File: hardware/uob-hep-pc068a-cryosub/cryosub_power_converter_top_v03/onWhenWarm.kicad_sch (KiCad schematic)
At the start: 15 parts, among them Q2 IRLML2402TRPBF

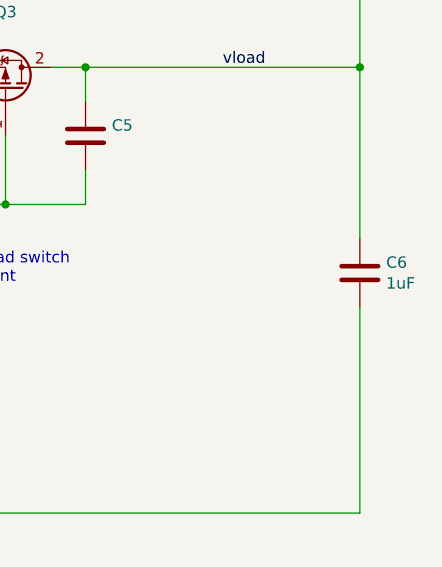
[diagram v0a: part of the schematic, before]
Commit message: Tweaked layout to remove DRCs (mainly silk) removed duplicate D1
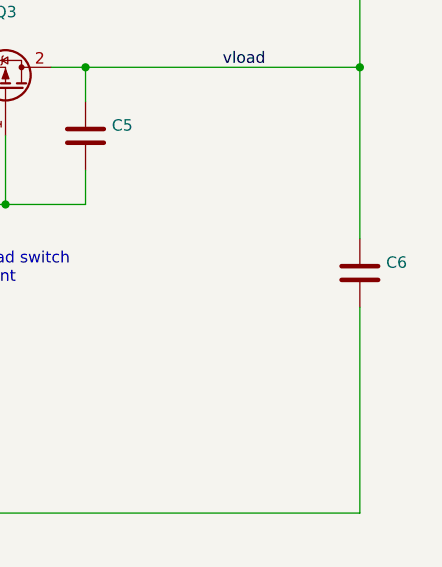
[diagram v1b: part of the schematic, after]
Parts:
- C5: footprint Capacitor_SMD:C_0603_1608Metric_Pad1.08x0.95mm_HandSolder -> (none)
- C6: value 1uF -> (none); footprint Capacitor_SMD:C_0805_2012Metric_Pad1.18x1.45mm_HandSolder -> (none)
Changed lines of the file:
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@@
       (effects (font (size 1.27 1.27)) (justify left))
     )
-    (property "Value" "1uF" (id 1) (at 267.081 97.663 0)
+    (property "Value" "" (id 1) (at 267.081 97.663 0)
       (effects (font (size 1.27 1.27)) (justify left))
     )
-    (property "Footprint" "Capacitor_SMD:C_0805_2012Metric_Pad1.18x1.45mm_HandSolder" (id 2) (at 265.1252 100.33 0)
+    (property "Footprint" "" (id 2) (at 265.1252 100.33 0)
       (effects (font (size 1.27 1.27)) hide)
     )
@@
       (effects (font (size 1.27 1.27)) (justify left))
     )
-    (property "Footprint" "Capacitor_SMD:C_0603_1608Metric_Pad1.08x0.95mm_HandSolder" (id 2) (at 234.6452 85.09 0)
+    (property "Footprint" "" (id 2) (at 234.6452 85.09 0)
       (effects (font (size 1.27 1.27)) hide)
     )

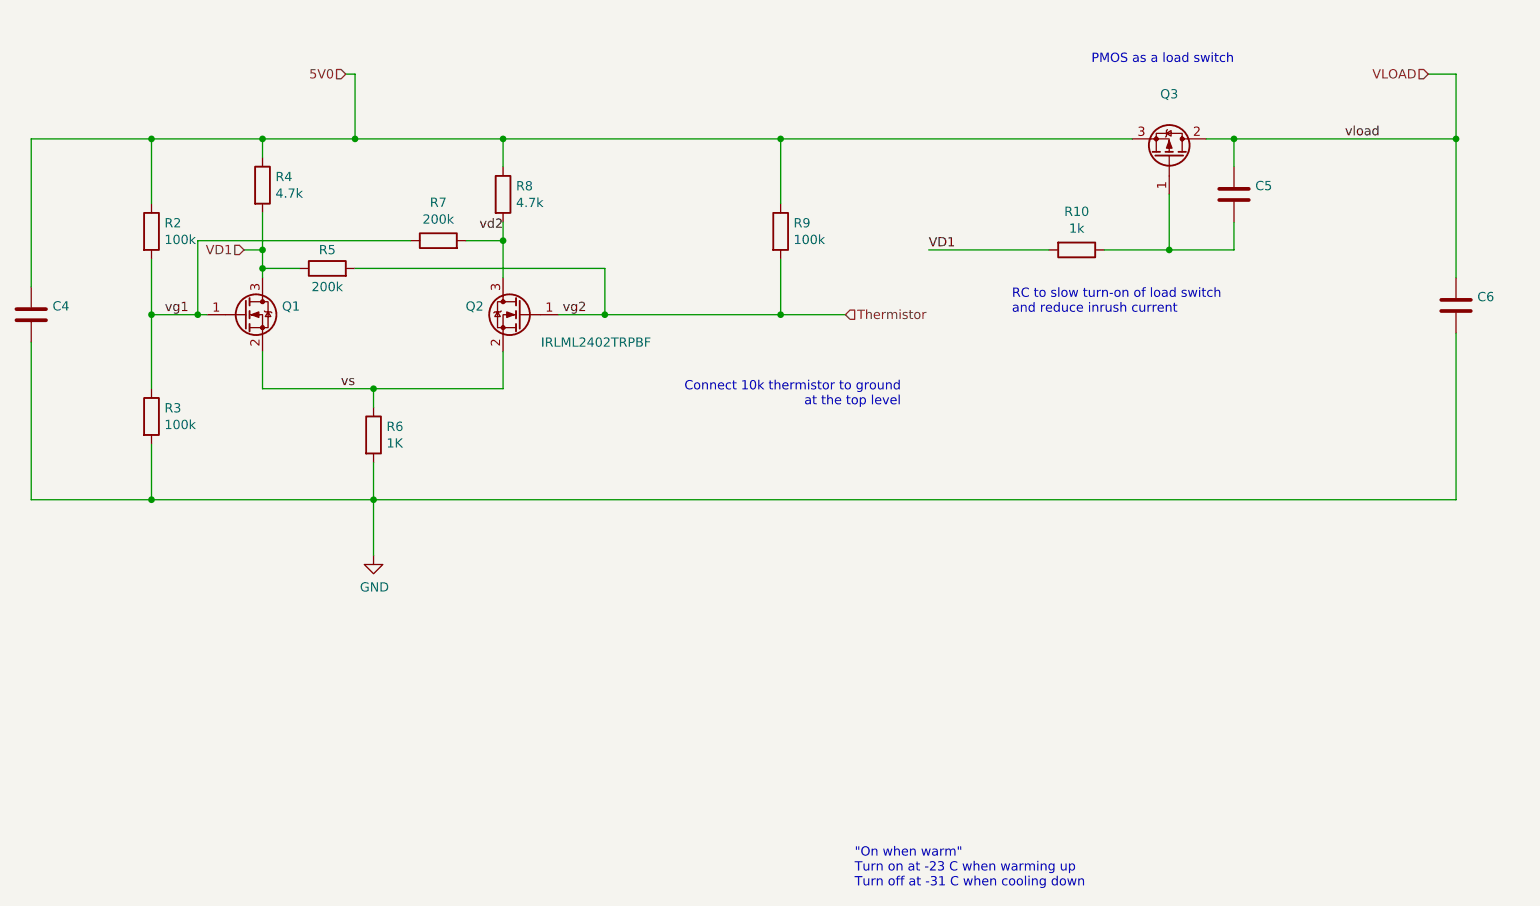
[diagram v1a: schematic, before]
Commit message: Replacing FDD306 with SiS407
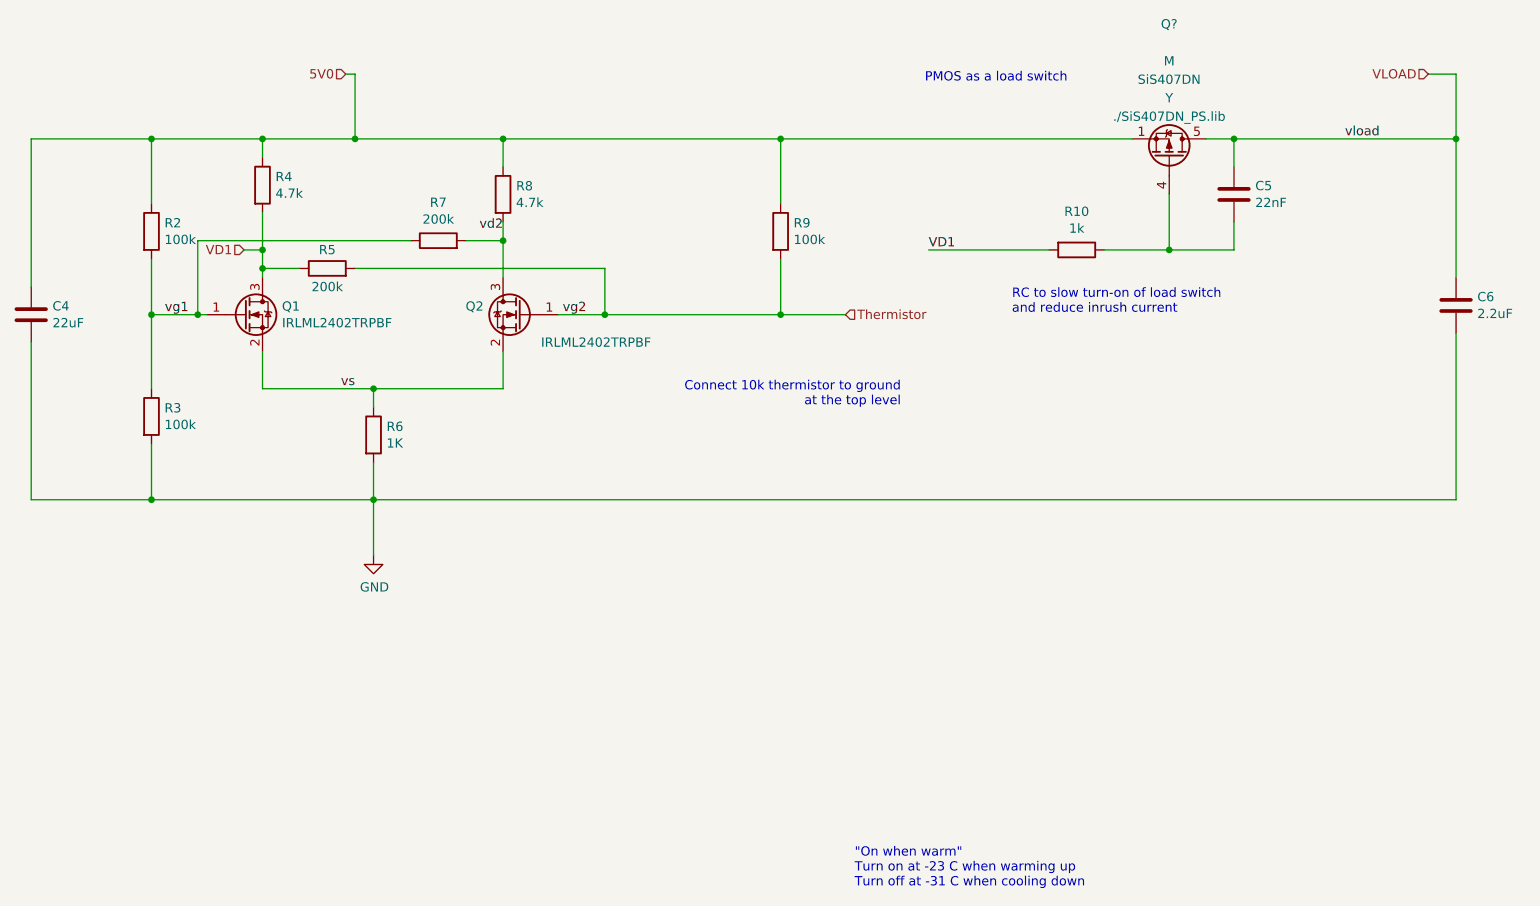
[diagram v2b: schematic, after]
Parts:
- removed Q3: (no value), symbol Device:Q_PMOS_GDS
- added Q?: (no value), symbol MOSFET:SiS407DN
- C4: value (none) -> 22uF; footprint (none) -> Capacitor_SMD:C_0805_2012Metric_Pad1.18x1.45mm_HandSolder
- C5: value (none) -> 22nF; footprint (none) -> Capacitor_SMD:C_0603_1608Metric
- C6: value (none) -> 2.2uF; footprint (none) -> Capacitor_SMD:C_0603_1608Metric
- Q1: value (none) -> IRLML2402TRPBF; footprint (none) -> Package_TO_SOT_SMD:SOT-23
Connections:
- net 5V0: now also Q?.1 (S), Q?.2 (S), Q?.3 (S)
- net VLOAD: now also Q?.5 (D)
- net at C5.2, R10.1: now also Q?.4 (G)
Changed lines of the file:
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@@
     (effects (font (size 1.27 1.27)) (justify right bottom))
   )
-  (text "PMOS as a load switch" (at 233.68 63.5 180)
+  (text "PMOS as a load switch" (at 210.82 66.04 180)
     (effects (font (size 1.27 1.27)) (justify right bottom))
   )
@@
       (effects (font (size 1.27 1.27)) (justify left))
     )
-    (property "Value" "" (id 1) (at 267.081 97.663 0)
-      (effects (font (size 1.27 1.27)) (justify left))
-    )
-    (property "Footprint" "" (id 2) (at 265.1252 100.33 0)
+    (property "Value" "2.2uF" (id 1) (at 267.081 97.663 0)
+      (effects (font (size 1.27 1.27)) (justify left))
+    )
+    (property "Footprint" "Capacitor_SMD:C_0603_1608Metric" (id 2) (at 265.1252 100.33 0)
       (effects (font (size 1.27 1.27)) hide)
     )
@@
       (effects (font (size 1.27 1.27)) (justify left))
     )
-    (property "Value" "" (id 1) (at 236.601 82.423 0)
-      (effects (font (size 1.27 1.27)) (justify left))
-    )
-    (property "Footprint" "" (id 2) (at 234.6452 85.09 0)
+    (property "Value" "22nF" (id 1) (at 236.601 82.423 0)
+      (effects (font (size 1.27 1.27)) (justify left))
+    )
+    (property "Footprint" "Capacitor_SMD:C_0603_1608Metric" (id 2) (at 234.6452 85.09 0)
       (effects (font (size 1.27 1.27)) hide)
     )
@@
       (effects (font (size 1.27 1.27)) (justify left))
     )
-    (property "Value" "" (id 1) (at 71.501 98.933 0)
-      (effects (font (size 1.27 1.27)) (justify left))
-    )
-    (property "Footprint" "" (id 2) (at 69.5452 101.6 0)
+    (property "Value" "22uF" (id 1) (at 71.501 98.933 0)
+      (effects (font (size 1.27 1.27)) (justify left))
+    )
+    (property "Footprint" "Capacitor_SMD:C_0805_2012Metric_Pad1.18x1.45mm_HandSolder" (id 2) (at 69.5452 101.6 0)
       (effects (font (size 1.27 1.27)) hide)
     )
@@
       (effects (font (size 1.27 1.27)) (justify left))
     )
-    (property "Value" "" (id 1) (at 102.997 98.933 0)
-      (effects (font (size 1.27 1.27)) (justify left))
-    )
-    (property "Footprint" "" (id 2) (at 102.87 99.695 0)
+    (property "Value" "IRLML2402TRPBF" (id 1) (at 102.997 98.933 0)
+      (effects (font (size 1.27 1.27)) (justify left))
+    )
+    (property "Footprint" "Package_TO_SOT_SMD:SOT-23" (id 2) (at 102.87 99.695 0)
       (effects (font (size 1.27 1.27) italic) (justify left) hide)
     )
@@
     (pin "2")
   )
-  (symbol (lib_id "Device:Q_PMOS_GDS") (at 224.79 76.2 270) (mirror x) (unit 1)
-    (in_bom yes) (on_board yes)
-    (property "Reference" "Q3" (id 0) (at 224.79 67.5132 90))
-    (property "Value" "" (id 1) (at 224.79 69.8246 90))
-    (property "Footprint" "" (id 2) (at 227.33 71.12 0)
-      (effects (font (size 1.27 1.27)) hide)
-    )
-    (property "Datasheet" "~" (id 3) (at 224.79 76.2 0)
-      (effects (font (size 1.27 1.27)) hide)
-    )
-    (property "Spice_Primitive" "X" (id 4) (at 224.79 76.2 0)
-      (effects (font (size 1.27 1.27)) hide)
-    )
-    (property "Spice_Model" "FDD306P" (id 5) (at 224.79 76.2 0)
-      (effects (font (size 1.27 1.27)) hide)
-    )
-    (property "Spice_Netlist_Enabled" "Y" (id 6) (at 224.79 76.2 0)
-      (effects (font (size 1.27 1.27)) hide)
-    )
-    (property "Spice_Lib_File" "./FDD306P.lib" (id 7) (at 224.79 76.2 0)
-      (effects (font (size 1.27 1.27)) hide)
-    )
-    (property "Spice_Node_Sequence" "2 1 3" (id 8) (at 224.79 76.2 0)
-      (effects (font (size 1.27 1.27)) hide)
-    )
-    (pin "1")
-    (pin "2")
-    (pin "3")
-  )
   (symbol (lib_id "Device:R") (at 212.09 88.9 270) (unit 1)
     (in_bom yes) (on_board yes)
@@
     (pin "1")
   )
+  (symbol (lib_id "MOSFET:SiS407DN") (at 224.79 76.2 270) (mirror x) (unit 1)
+    (in_bom yes) (on_board yes) (fields_autoplaced)
+    (property "Reference" "Q?" (id 0) (at 224.79 57.9076 90))
+    (property "Value" "" (id 1) (at 224.79 60.4445 90))
+    (property "Footprint" "" (id 2) (at 222.885 71.12 0)
+      (effects (font (size 1.27 1.27) italic) (justify left) hide)
+    )
+    (property "Datasheet" "https://www.vishay.com/docs/65942/sis407dn.pdf" (id 3) (at 224.79 76.2 90)
+      (effects (font (size 1.27 1.27)) (justify left) hide)
+    )
+    (property "Spice_Primitive" "M" (id 4) (at 224.79 62.9814 90))
+    (property "Spice_Model" "SiS407DN" (id 5) (at 224.79 65.5183 90))
+    (property "Spice_Netlist_Enabled" "Y" (id 6) (at 224.79 68.0552 90))
+    (property "Spice_Lib_File" "./SiS407DN_PS.lib" (id 7) (at 224.79 70.5921 90))
+    (pin "1")
+    (pin "2")
+    (pin "3")
+    (pin "4")
+    (pin "5")
+  )
 )

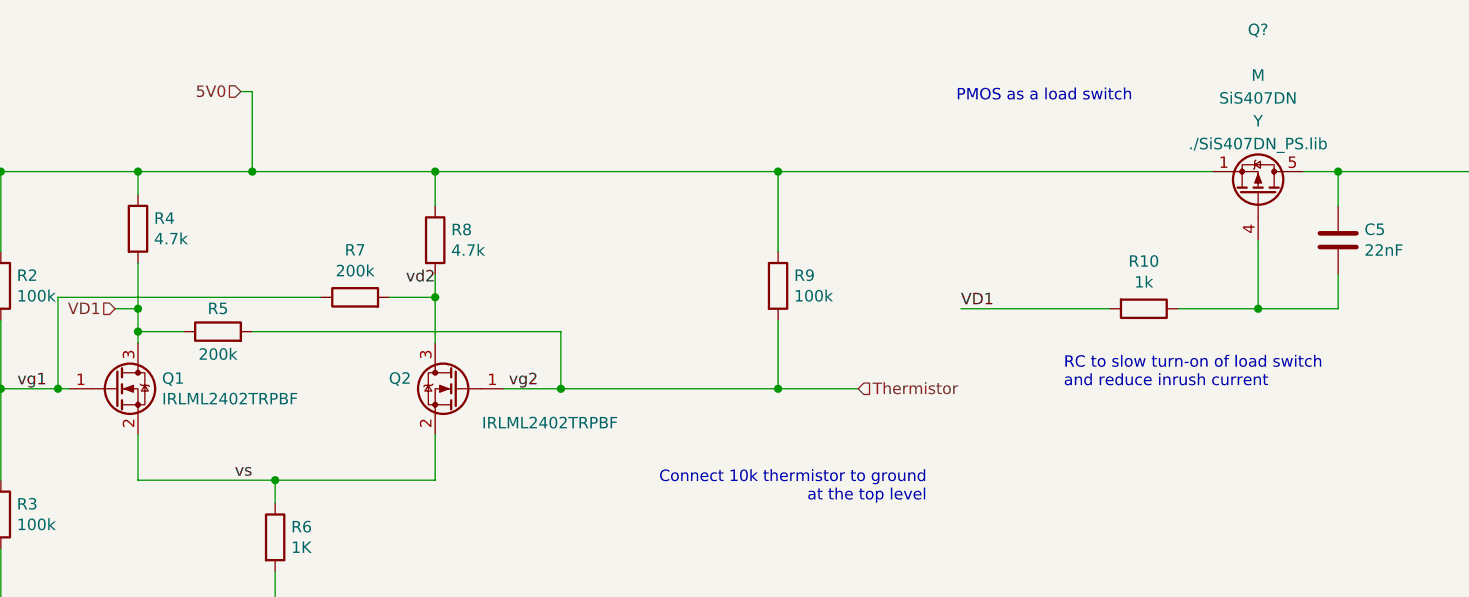
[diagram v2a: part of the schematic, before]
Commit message: Updated schematic with irlml2402 --> irlml2803 , fdd306 --> sis407 to cope with component shortage. Updated PCB
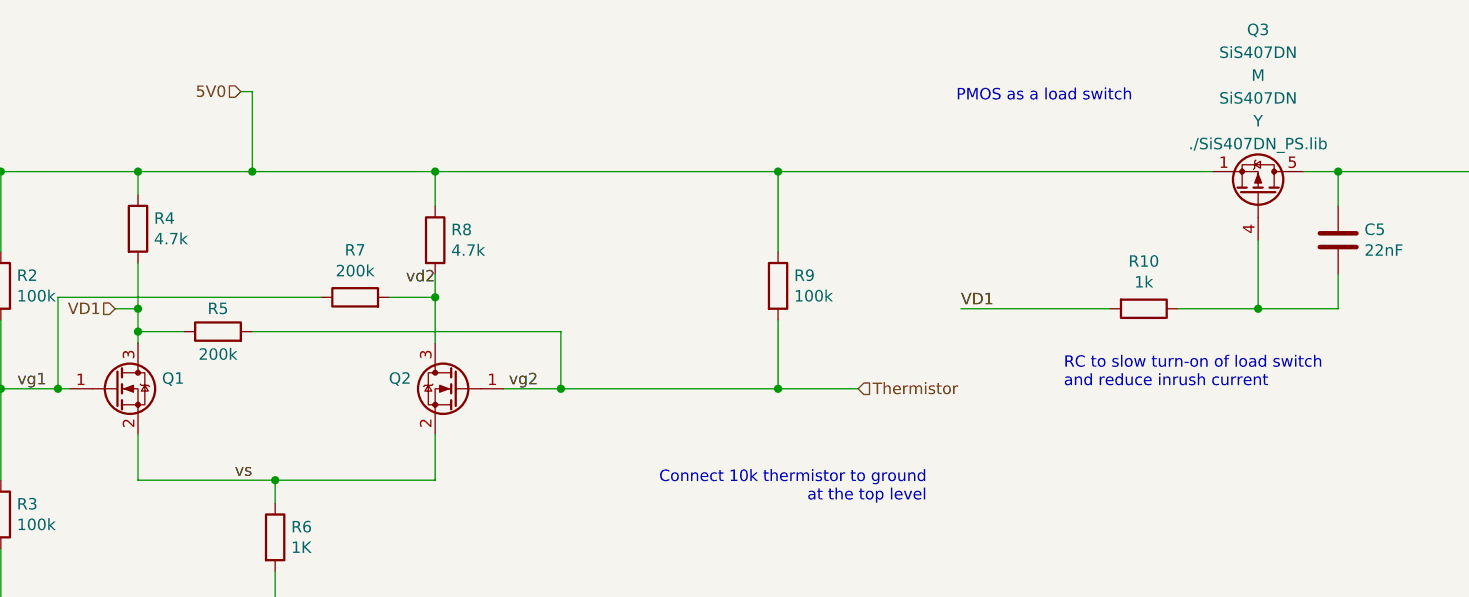
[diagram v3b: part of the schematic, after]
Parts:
- Q1, Q2: value IRLML2402TRPBF -> (none); footprint Package_TO_SOT_SMD:SOT-23 -> (none)
- Q3: renamed from Q?; value (none) -> SiS407DN; footprint (none) -> Package_SO:Vishay_PowerPAK_1212-8_Single
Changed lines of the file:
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@@
       (effects (font (size 1.27 1.27)) (justify left))
     )
-    (property "Value" "IRLML2402TRPBF" (id 1) (at 102.997 98.933 0)
+    (property "Value" "" (id 1) (at 102.997 98.933 0)
       (effects (font (size 1.27 1.27)) (justify left))
     )
-    (property "Footprint" "Package_TO_SOT_SMD:SOT-23" (id 2) (at 102.87 99.695 0)
+    (property "Footprint" "" (id 2) (at 102.87 99.695 0)
       (effects (font (size 1.27 1.27) italic) (justify left) hide)
     )
@@
       (effects (font (size 1.27 1.27)) (justify left))
     )
-    (property "Value" "IRLML2402TRPBF" (id 1) (at 153.67 101.6 0)
+    (property "Value" "" (id 1) (at 153.67 101.6 0)
       (effects (font (size 1.27 1.27)) (justify left))
     )
-    (property "Footprint" "Package_TO_SOT_SMD:SOT-23" (id 2) (at 130.81 99.695 0)
+    (property "Footprint" "" (id 2) (at 130.81 99.695 0)
       (effects (font (size 1.27 1.27) italic) (justify left) hide)
     )
@@
   (symbol (lib_id "MOSFET:SiS407DN") (at 224.79 76.2 270) (mirror x) (unit 1)
     (in_bom yes) (on_board yes) (fields_autoplaced)
-    (property "Reference" "Q?" (id 0) (at 224.79 57.9076 90))
-    (property "Value" "" (id 1) (at 224.79 60.4445 90))
-    (property "Footprint" "" (id 2) (at 222.885 71.12 0)
+    (property "Reference" "Q3" (id 0) (at 224.79 57.9076 90))
+    (property "Value" "SiS407DN" (id 1) (at 224.79 60.4445 90))
+    (property "Footprint" "Package_SO:Vishay_PowerPAK_1212-8_Single" (id 2) (at 222.885 71.12 0)
       (effects (font (size 1.27 1.27) italic) (justify left) hide)
     )
